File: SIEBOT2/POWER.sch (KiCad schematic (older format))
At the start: 0 parts

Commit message: Added power dc-dc, fixed stm32 control pins
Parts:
- added C14: 220n, symbol C
- added C15: 10n, symbol C
- added C16: 220uF-16V, symbol CP1
- added D1: LED, symbol LED
- added L1: IHLP2525CZER8R2M01, symbol IHLP2525CZER8R2M01
- added P6: CONN_2X2, symbol CONN_2X2
- added R10: 0.015, symbol R
- added R3, R4: 1K, symbol R
- added R5: 8.66K, symbol R
- added R6: 604, symbol R
- added R7: 1k, symbol R
- added R8: 56.2K, symbol R
- added R9: 0, symbol R
- added U2: LM3478, symbol LM3478
- added U3: IRF8113, symbol IRF8113
- added U4: MBRD1035CTL, symbol MBRD1035CTL
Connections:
- new net: R4.1, R5.2, U2.3 (FB)
- new net: L1.2, U3.5 (D), U3.6 (D), U3.7 (D), U3.8 (D), U4.1, U4.3
- new net: R6.2, U2.1 (ISEN)
- new net: R3.1, U2.2 (COMP)
- new net: R9.2, U2.6 (DR)
- new net: R8.2, U2.7 (FA/SD)
- new net: C15.1, R10.1, R6.1, U3.1 (S), U3.2 (S), U3.3 (S)
- new net: R9.1, U3.4 (G)
- new net: C14.1, R3.2
- new net: D1.2 (K), R7.2
- new net GND: C14.2, C15.2, C16.2, P6.3, P6.4, R10.2, R4.2, R7.1, R8.1, U2.4 (AGND), U2.5 (PGND)
- new net POWER_12V: C16.1, R5.1, U4.4
- new net POWER_BATT: L1.1, U2.8 (VIN)
- new net VDD5V: D1.1 (A), P6.1, P6.2
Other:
- note added: "DC-DC converter 12V output"
- note added: "Power Supply"

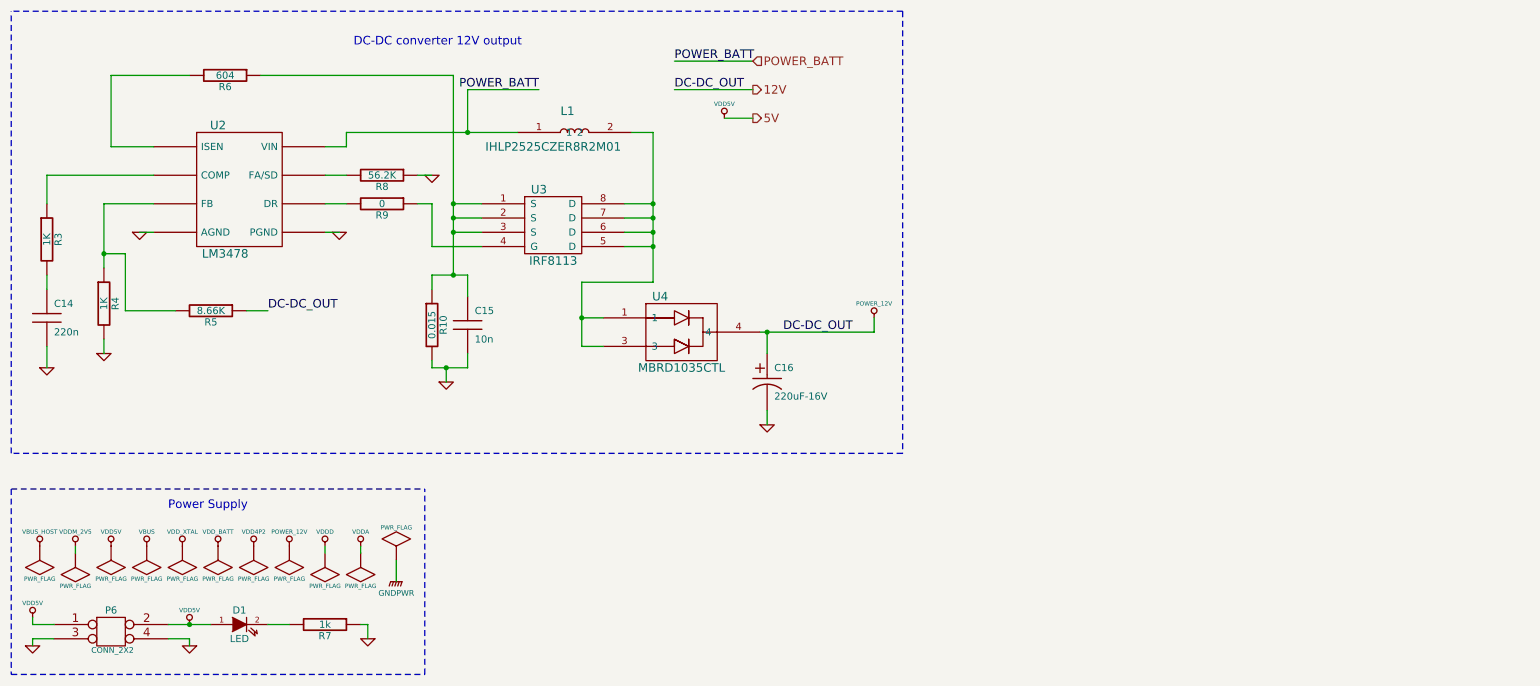
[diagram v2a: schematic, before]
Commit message: STM32 connection fixes + various fixes
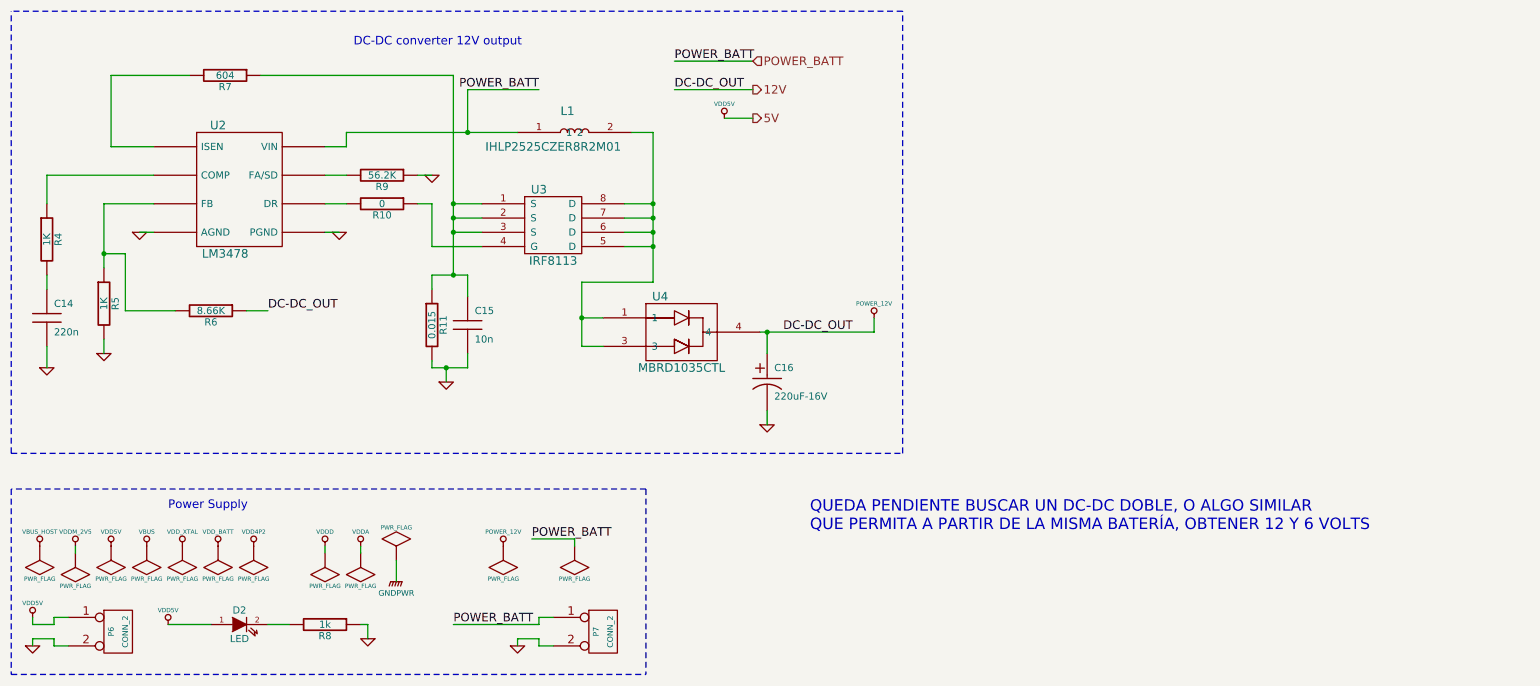
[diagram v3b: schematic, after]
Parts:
- removed P6: CONN_2X2, symbol CONN_2X2
- added P6, P7: CONN_2, symbol CONN_2
- renumbered D1 to D2, R9 to R10, R10 to R11, R3 to R4, R4 to R5, R5 to R6, R6 to R7, R7 to R8, R8 to R9
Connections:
- net GND: now also P6.2 (PM), P7.2 (PM)
- net POWER_BATT: now also P7.1 (P1)
- net VDD5V: now also P6.1 (P1)
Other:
- note added: "QUEDA PENDIENTE BUSCAR UN DC-DC DOBLE, O ALGO SIMILAR \nQUE PERMITA A PARTIR DE LA MISMA BATERÍA, OBTENER 12 Y 6 VOLTS"
